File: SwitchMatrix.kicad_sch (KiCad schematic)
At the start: 166 parts, among them SW1 1u, SW10 1u, SW11 1u, SW12 1u, SW13 1u, SW14 1u, SW15 1u, SW16 1u, SW17 2u, SW18 1.5u, SW19 1u, SW2 1u, SW20 1u, SW21 1u, SW22 1u, SW23 1u, SW24 1u, SW25 1u, SW26 1u, SW27 1u, SW28 1u, SW29 1u, SW3 1u, SW30 1u, SW31 1.5u, SW32 ISO Enter, SW33 1u, SW34 1.25u, SW35 1.75u, SW36 1u, SW37 1u, SW38 1u, SW39 1u, SW4 1u, SW40 1u, SW41 1u, SW42 1u, SW43 1u, SW44 1u, SW45 1u, SW46 1u, SW47 2.25u, SW48 1u, SW49 1u, SW5 1u, SW50 2.25u, SW51 1.25u, SW52 1u, SW53 1u, SW54 1u, SW55 1u, SW56 1u, SW57 1u, SW58 1u, SW59 1u, SW6 1u, SW60 1u, SW61 1u, SW62 1u, SW63 1.75u, SW64 1u, SW65 1u, SW66 1.5u, SW67 1.25u, SW68 1u, SW69 1.25u, SW7 1u, SW70 1.5u, SW71 1.25u, SW72 3u, SW73 7u, SW74 6.25u, SW75 3u, SW76 1.25u, SW77 1.5u, SW78 1.25u, SW79 1u, SW8 1u, SW80 1u, SW81 1u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

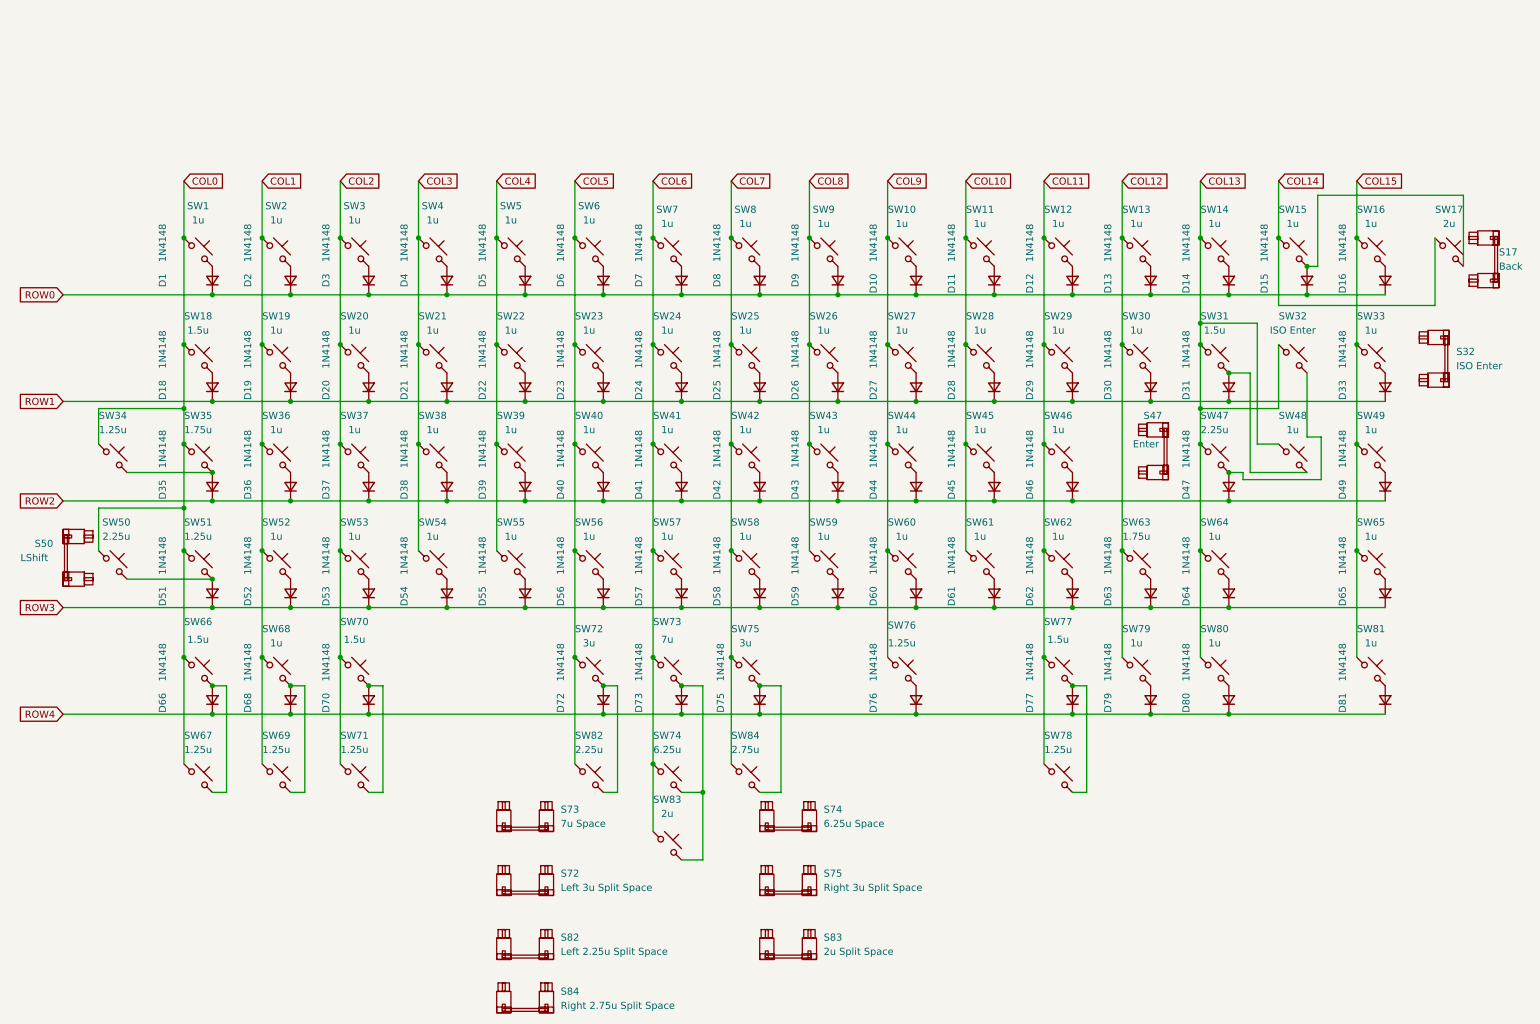
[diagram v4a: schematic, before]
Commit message: second (unsuccessful) attempt to fix stabs
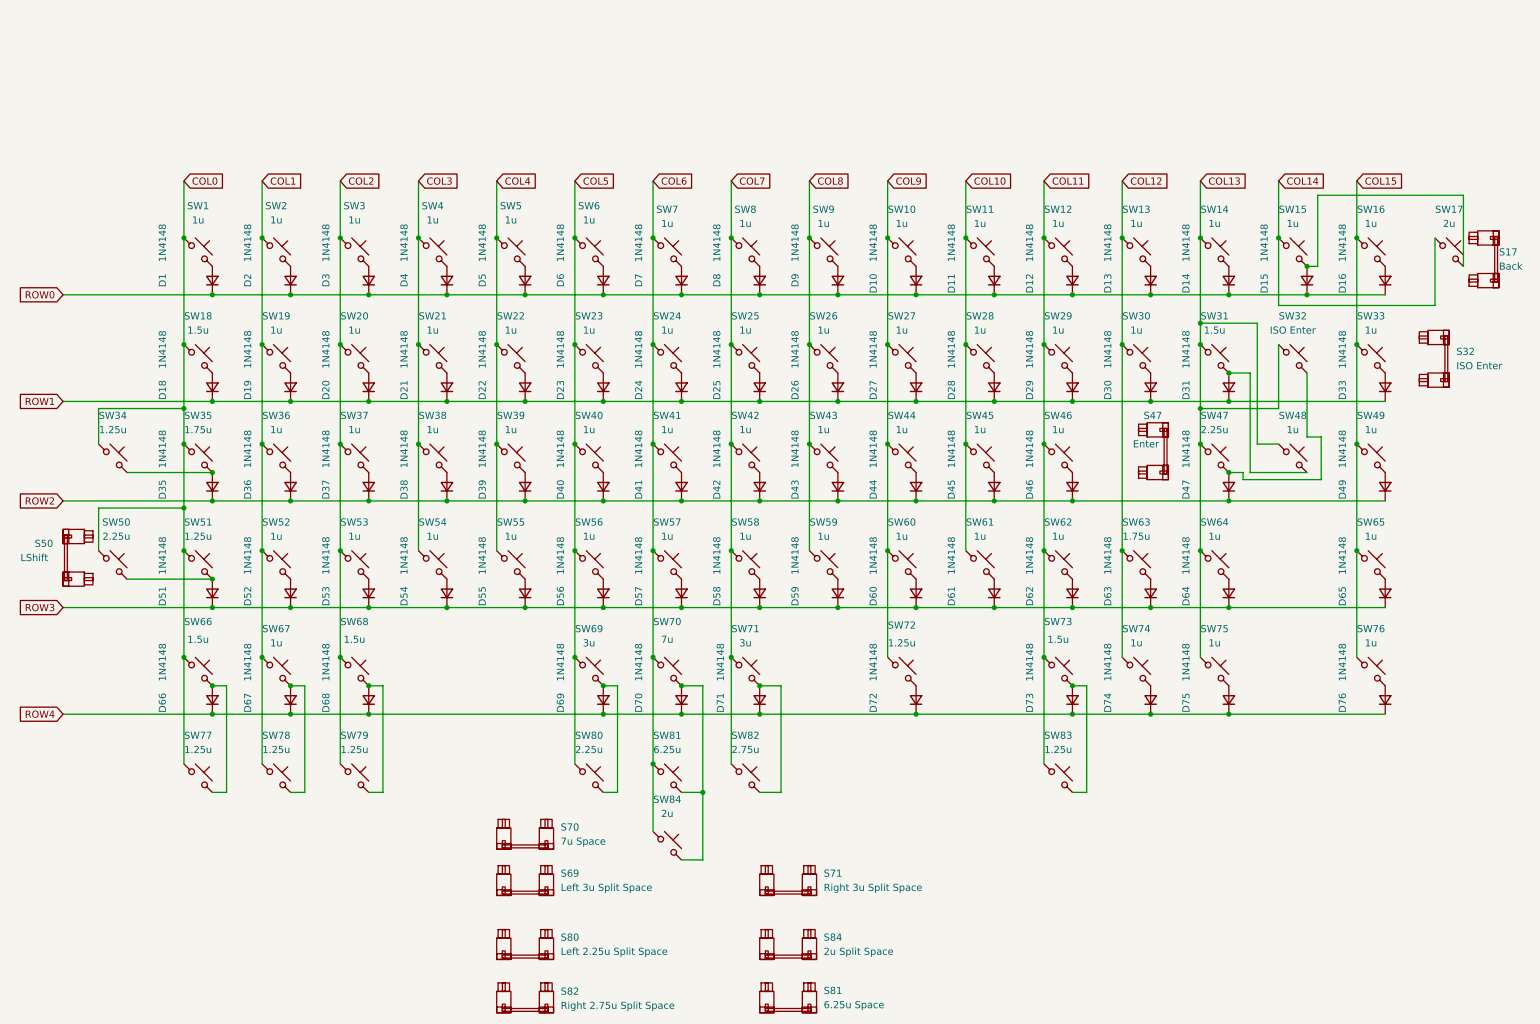
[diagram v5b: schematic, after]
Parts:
- renumbered D68 to D67, D70 to D68, D72 to D69, D73 to D70, D75 to D71, D76 to D72, D77 to D73, D79 to D74, D80 to D75, D81 to D76, S72 to S69, S73 to S70, S75 to S71, S82 to S80, S74 to S81, S84 to S82, S83 to S84, SW68 to SW67, SW70 to SW68, SW72 to SW69, SW73 to SW70, SW75 to SW71, SW76 to SW72, SW77 to SW73, SW79 to SW74, SW80 to SW75, SW81 to SW76, SW67 to SW77, SW69 to SW78, SW71 to SW79, SW82 to SW80, SW74 to SW81, SW84 to SW82, SW78 to SW83, SW83 to SW84
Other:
- moved on the sheet: S70, S81

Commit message: third unsuccessful stab fix
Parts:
- renumbered D67 to D68, D68 to D70, D69 to D72, D70 to D74, D71 to D77, D72 to D79, D73 to D80, D74 to D82, D75 to D83, D76 to D84, S69 to S72, S80 to S73, S70 to S74, S81 to S75, S84 to S76, S71 to S77, S82 to S78, SW77 to SW67, SW67 to SW68, SW78 to SW69, SW68 to SW70, SW79 to SW71, SW69 to SW72, SW80 to SW73, SW70 to SW74, SW81 to SW75, SW84 to SW76, SW71 to SW77, SW82 to SW78, SW72 to SW79, SW73 to SW80, SW83 to SW81, SW74 to SW82, SW75 to SW83, SW76 to SW84

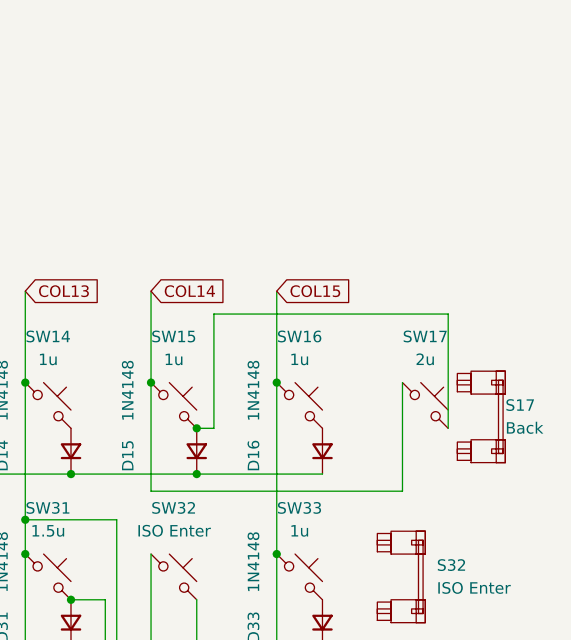
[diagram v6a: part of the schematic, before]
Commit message: Assign footprints, add knob symbol
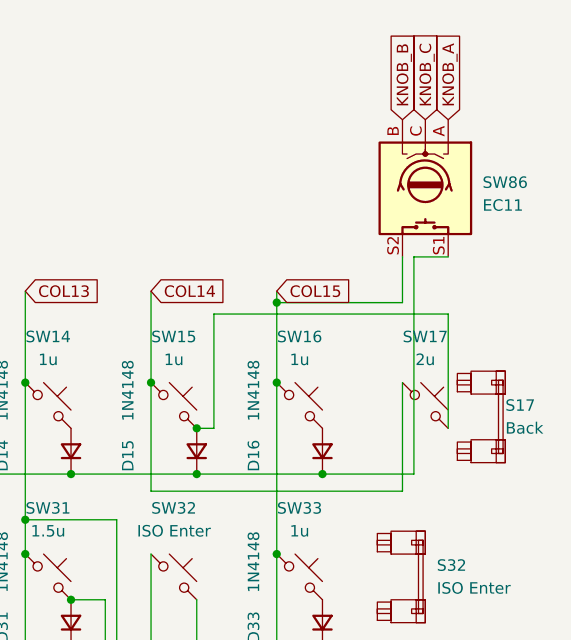
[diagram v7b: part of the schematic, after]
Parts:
- added SW86: EC11, Rotary_Encoder:RotaryEncoder_Alps_EC11E-Switch_Vertical_H20mm, symbol Device:RotaryEncoder_Switch
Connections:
- net COL15: now also SW86.S2
- net ROW0: now also SW86.S1
- new net KNOB_A: SW86.A
- new net KNOB_B: SW86.B
- new net KNOB_C: SW86.C

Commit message: replacing MCU, some col traces
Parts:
- S17, S76: footprint marbastlib-mx:STAB_MX_2u -> marbastlib-mx:STAB_MX_P_2u
- S47, S50, S73: footprint marbastlib-mx:STAB_MX_2.25u -> marbastlib-mx:STAB_MX_P_2.25u
- S72, S77: footprint marbastlib-mx:STAB_MX_3u -> marbastlib-mx:STAB_MX_P_3u
- S74: footprint marbastlib-mx:STAB_MX_7u -> marbastlib-mx:STAB_MX_P_7u
- S75: footprint marbastlib-mx:STAB_MX_6.25u -> marbastlib-mx:STAB_MX_P_6.25u
- S78: footprint marbastlib-mx:STAB_MX_2.75u -> marbastlib-mx:STAB_MX_P_2.75u
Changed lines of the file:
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@@
       (effects (font (size 1.27 1.27)) (justify left))
     )
-    (property "Footprint" "marbastlib-mx:STAB_MX_3u" (at 149.86 168.275 0)
+    (property "Footprint" "marbastlib-mx:STAB_MX_P_3u" (at 149.86 168.275 0)
       (effects (font (size 1.27 1.27)) hide)
     )
@@
       (effects (font (size 1.27 1.27)) (justify left))
     )
-    (property "Footprint" "marbastlib-mx:STAB_MX_2.25u" (at 22.86 110.49 0)
+    (property "Footprint" "marbastlib-mx:STAB_MX_P_2.25u" (at 22.86 110.49 0)
       (effects (font (size 1.27 1.27)) hide)
     )
@@
       (effects (font (size 1.27 1.27)) (justify left))
     )
-    (property "Footprint" "marbastlib-mx:STAB_MX_2.25u" (at 102.87 179.705 0)
+    (property "Footprint" "marbastlib-mx:STAB_MX_P_2.25u" (at 102.87 179.705 0)
       (effects (font (size 1.27 1.27)) hide)
     )
@@
       (effects (font (size 1.27 1.27)) (justify left))
     )
-    (property "Footprint" "marbastlib-mx:STAB_MX_6.25u" (at 149.86 189.23 0)
+    (property "Footprint" "marbastlib-mx:STAB_MX_P_6.25u" (at 149.86 189.23 0)
       (effects (font (size 1.27 1.27)) hide)
     )
@@
       (effects (font (size 1.27 1.27)) (justify left))
     )
-    (property "Footprint" "marbastlib-mx:STAB_MX_7u" (at 102.87 160.02 0)
+    (property "Footprint" "marbastlib-mx:STAB_MX_P_7u" (at 102.87 160.02 0)
       (effects (font (size 1.27 1.27)) hide)
     )
@@
       (effects (font (size 1.27 1.27)) (justify right))
     )
-    (property "Footprint" "marbastlib-mx:STAB_MX_2u" (at 274.32 57.15 0)
+    (property "Footprint" "marbastlib-mx:STAB_MX_P_2u" (at 274.32 57.15 0)
       (effects (font (size 1.27 1.27)) hide)
     )
@@
       (effects (font (size 1.27 1.27)) (justify left))
     )
-    (property "Footprint" "marbastlib-mx:STAB_MX_2u" (at 149.86 179.705 0)
+    (property "Footprint" "marbastlib-mx:STAB_MX_P_2u" (at 149.86 179.705 0)
       (effects (font (size 1.27 1.27)) hide)
     )
@@
       (effects (font (size 1.27 1.27)) (justify left))
     )
-    (property "Footprint" "marbastlib-mx:STAB_MX_3u" (at 102.87 168.275 0)
+    (property "Footprint" "marbastlib-mx:STAB_MX_P_3u" (at 102.87 168.275 0)
       (effects (font (size 1.27 1.27)) hide)
     )
@@
       (effects (font (size 1.27 1.27)) (justify left))
     )
-    (property "Footprint" "marbastlib-mx:STAB_MX_2.75u" (at 102.87 189.23 0)
+    (property "Footprint" "marbastlib-mx:STAB_MX_P_2.75u" (at 102.87 189.23 0)
       (effects (font (size 1.27 1.27)) hide)
     )
@@
       (effects (font (size 1.27 1.27)) (justify right))
     )
-    (property "Footprint" "marbastlib-mx:STAB_MX_2.25u" (at 215.265 91.44 0)
-      (effects (font (size 1.27 1.27)) hide)
-    )
+    (property "Footprint" "marbastlib-mx:STAB_MX_P_2.25u" (at 215.265 91.44 0)
+      (effects (font (size 1.27 1.27)) hide)
+    )
